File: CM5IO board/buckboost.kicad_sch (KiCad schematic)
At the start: 4 parts, among them IC1 TPS61089RNRR

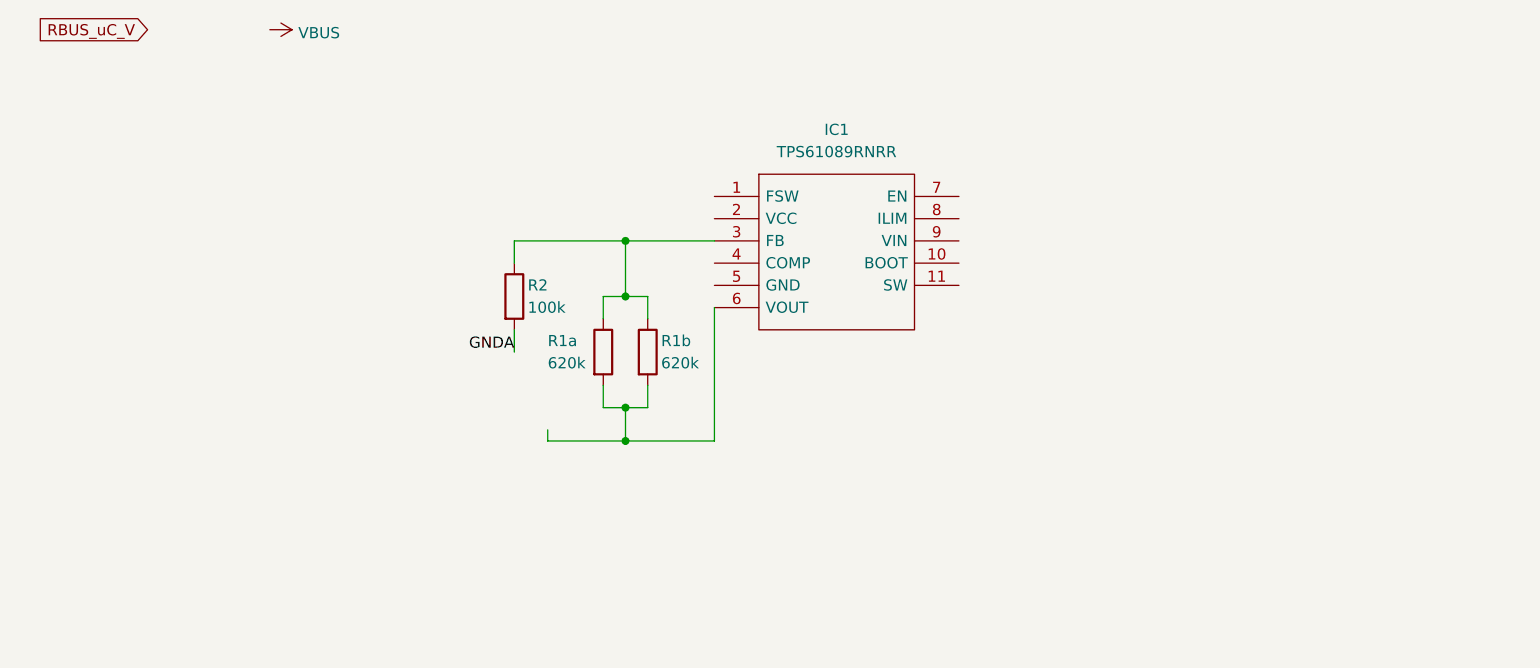
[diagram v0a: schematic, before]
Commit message: Continued boost design
R4, C1, C2, C3 selected
R4, L1 unsure
COMP, EN yet to be finished.
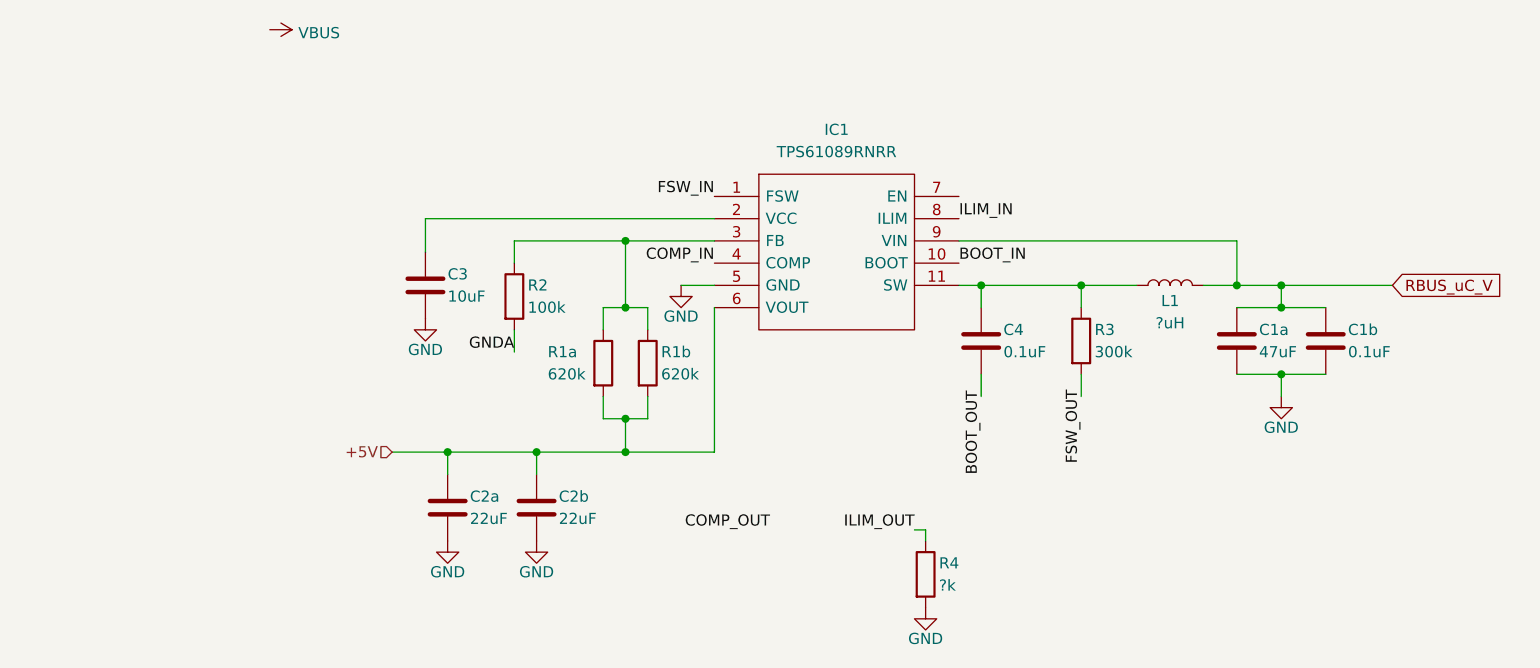
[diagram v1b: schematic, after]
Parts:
- added C1a: 47uF, symbol Device:C
- added C1b, C4: 0.1uF, symbol Device:C
- added C2a, C2b: 22uF, symbol Device:C
- added C3: 10uF, symbol Device:C
- added L1: ?uH, symbol Device:L
- added R3: 300k, symbol Device:R
- added R4: ?k, symbol Device:R
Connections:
- net RBUS_uC_V: now also IC1.9 (VIN), C1a.1, C1b.1, L1.2
- net +5V: now reaches IC1.6 (VOUT), R1a.2, R1b.2
- net +5V: now also C2a.1, C2b.1
- net FSW_IN: now reaches IC1.1 (FSW)
- net BOOT_IN: now reaches IC1.10 (BOOT)
- net at IC1.11 (SW): now also C4.1, L1.1, R3.1
- net at IC1.2 (VCC): now also C3.1
- net COMP_IN: now reaches IC1.4 (COMP)
- net GND: now reaches IC1.5 (GND)
- net GND: now also C1a.2, C1b.2, C2a.2, C2b.2, C3.2, R4.2
- net ILIM_IN: now reaches IC1.8 (ILIM)
- new net ILIM_OUT: R4.1
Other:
- moved on the sheet: R1a, R1b

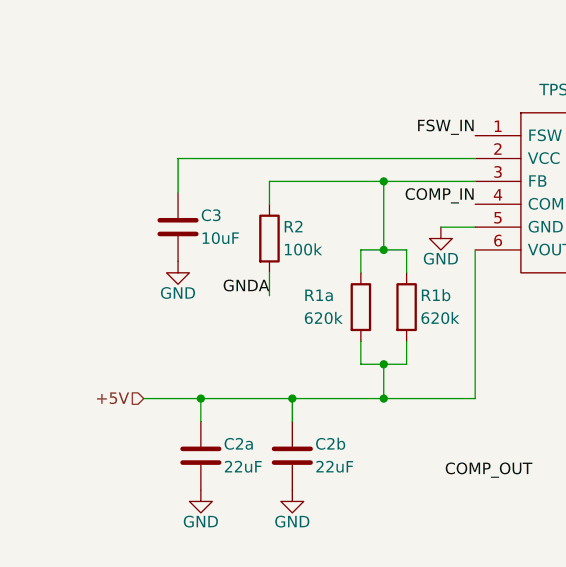
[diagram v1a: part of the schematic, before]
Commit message: C3 GND -> GNDA
small mistake
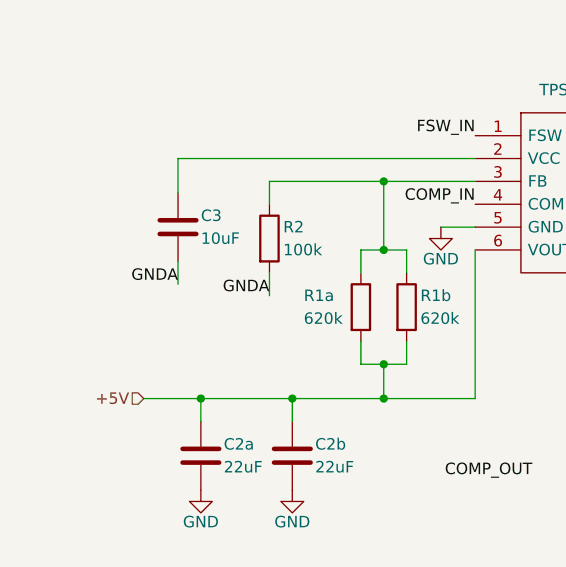
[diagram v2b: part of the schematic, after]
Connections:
- net GND: no longer C3.2
- net GNDA: now also C3.2
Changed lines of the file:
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@@
+	(wire
+		(pts
+			(xy 87.63 82.55) (xy 87.63 85.09)
+		)
+		(stroke
+			(width 0)
+			(type default)
+		)
+	)
 	(wire
 		(pts
@@
 			(width 0)
 			(type default)
+		)
+	)
+	(label "GNDA"
+		(at 87.63 85.09 180)
+		(effects
+			(font
+				(size 1.27 1.27)
+			)
+			(justify right bottom)
 		)
 	)
@@
 					(unit 1)
 				)
-			)
-		)
-	)
-	(symbol
-		(lib_id "power:GND")
-		(at 87.63 82.55 0)
-		(unit 1)
-		(exclude_from_sim no)
-		(in_bom yes)
-		(on_board yes)
-		(dnp no)
-		(property "Reference" "#PWR031"
-			(at 87.63 88.9 0)
-			(effects
-				(font
-					(size 1.27 1.27)
-				)
-				(hide yes)
-			)
-		)
-		(property "Value" "GND"
-			(at 87.63 86.106 0)
-			(effects
-				(font
-					(size 1.27 1.27)
-				)
-			)
-		)
-		(property "Footprint" ""
-			(at 87.63 82.55 0)
-			(effects
-				(font
-					(size 1.27 1.27)
-				)
-				(hide yes)
-			)
-		)
-		(property "Datasheet" ""
-			(at 87.63 82.55 0)
-			(effects
-				(font
-					(size 1.27 1.27)
-				)
-				(hide yes)
-			)
-		)
-		(property "Description" "Power symbol creates a global label with name \"GND\" , ground"
-			(at 87.63 82.55 0)
-			(effects
-				(font
-					(size 1.27 1.27)
-				)
-				(hide yes)
-			)
-		)
-		(pin "1"
-		)
-		(instances
-			(project "CM5IO"
-				(path "/e63e39d7-6ac0-4ffd-8aa3-1841a4541b55/10bbbb5c-8f12-4f88-ba95-995cc19aee5f"
-					(reference "#PWR031")
-					(unit 1)
-				)

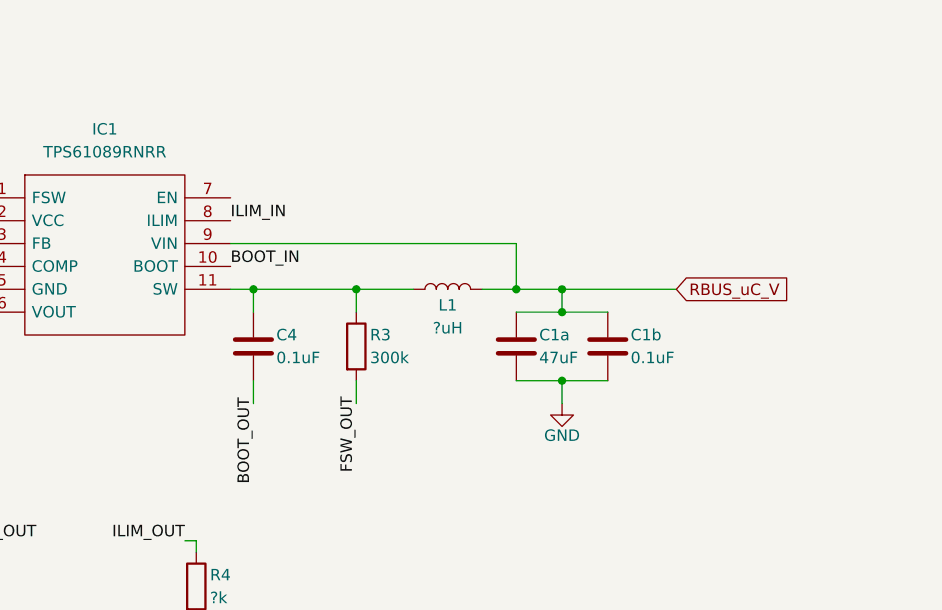
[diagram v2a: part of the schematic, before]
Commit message: EN L1 completed
R_EN set to 800k (typ) (could be 10k) | L1 set to 2.2uH (744311220 Wurth); imported to iclr-hw
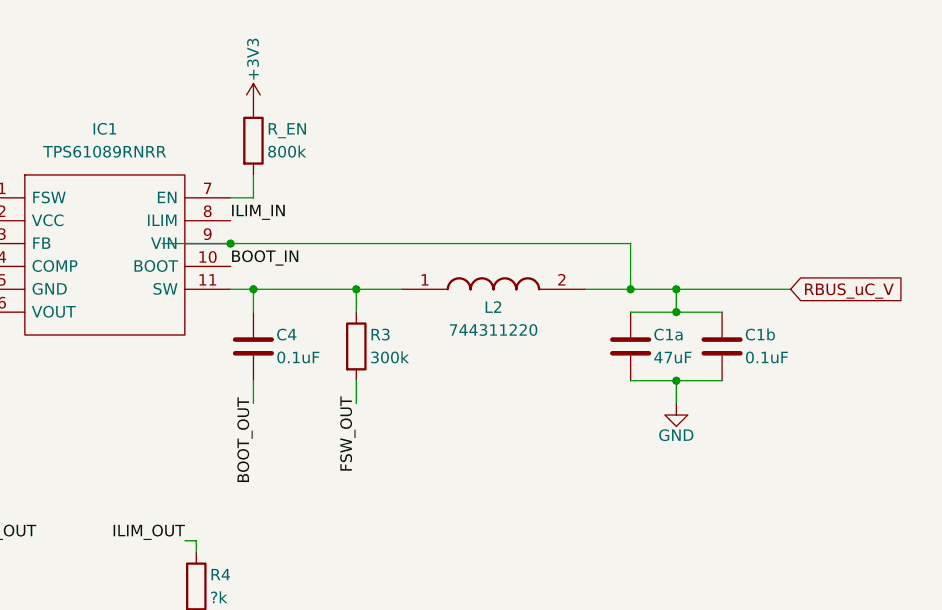
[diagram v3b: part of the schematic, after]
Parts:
- removed L1: ?uH, symbol Device:L
- added L2: 744311220, WE-HCI_7030/7040/705023, symbol iclr:744311220
- added R_EN: 800k, symbol Device:R
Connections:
- net RBUS_uC_V: now also L2.2
- net at C4.1, IC1.11 (SW), R3.1: now also L2.1
- net at IC1.7 (EN): now also R_EN.2
- new net +3V3: R_EN.1
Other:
- moved on the sheet: C1a, C1b

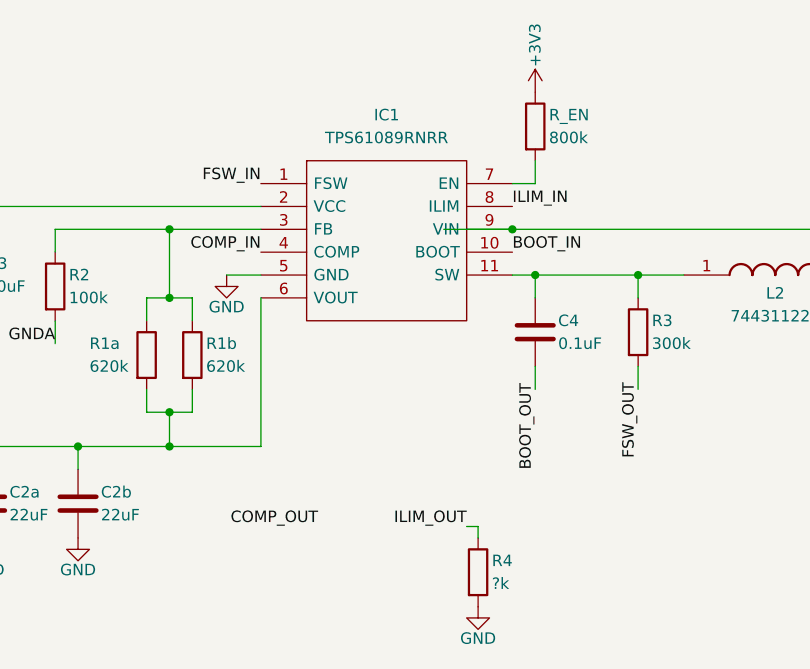
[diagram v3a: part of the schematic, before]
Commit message: Edited I/O port names for consistency
e.g. FSW_IN & FSW_OUT -> FSW_IO
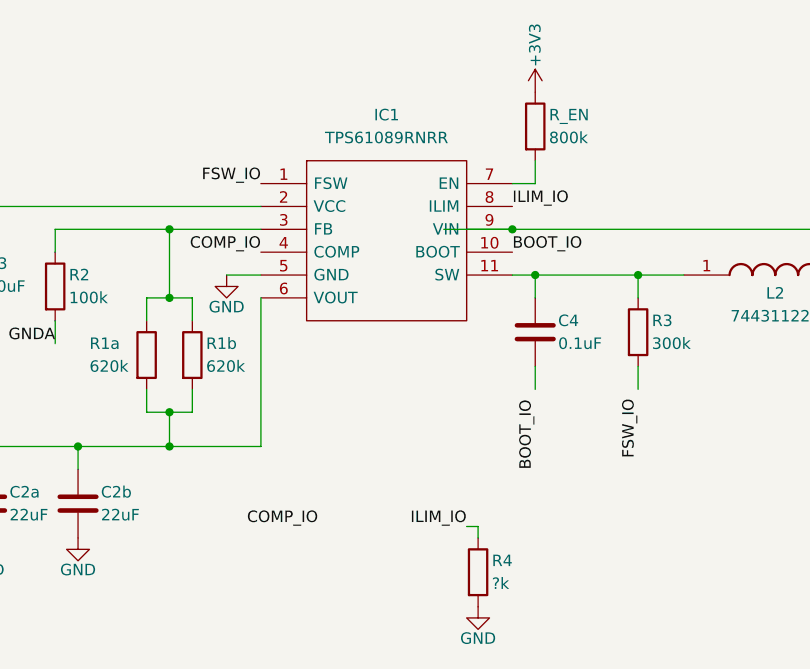
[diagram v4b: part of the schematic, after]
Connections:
- net ILIM_OUT is gone; now on net ILIM_IO: R4.1
- net BOOT_IN renamed BOOT_IO
- net COMP_IN renamed COMP_IO
- net FSW_IN renamed FSW_IO
- net ILIM_IN renamed ILIM_IO
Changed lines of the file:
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@@
 		)
 	)
-	(label "ILIM_OUT"
+	(label "ILIM_IO"
 		(at 143.51 106.68 180)
 		(effects
@@
 		)
 	)
-	(label "FSW_OUT"
+	(label "FSW_IO"
 		(at 162.56 99.06 90)
 		(effects
@@
 		)
 	)
-	(label "ILIM_IN"
+	(label "ILIM_IO"
 		(at 148.59 71.12 0)
 		(effects
@@
 		)
 	)
-	(label "FSW_IN"
+	(label "FSW_IO"
 		(at 120.65 68.58 180)
 		(effects
@@
 		)
 	)
-	(label "BOOT_OUT"
+	(label "BOOT_IO"
 		(at 151.13 100.33 90)
 		(effects
@@
 		)
 	)
-	(label "COMP_IN"
+	(label "COMP_IO"
 		(at 120.65 76.2 180)
 		(effects
@@
 		)
 	)
-	(label "BOOT_IN"
+	(label "BOOT_IO"
 		(at 148.59 76.2 0)
 		(effects
@@
 		)
 	)
-	(label "COMP_OUT"
+	(label "COMP_IO"
 		(at 127 106.68 180)
 		(effects
